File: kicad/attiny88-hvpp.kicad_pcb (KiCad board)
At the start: 2 copper layers, 77 x 58.7 mm, 15 parts, among them J1 12v_reg_left_neg, J2 12v_reg_right_pos, J3 purle_pi_left, J4 purle_pi_right, J5 ATTINY88_LEFT, J6 ATTINY88_RIGHT, Q1 MMBT3904, Q2 IRLML6402, Q3 MMBT3904, Q4 IRLML6402

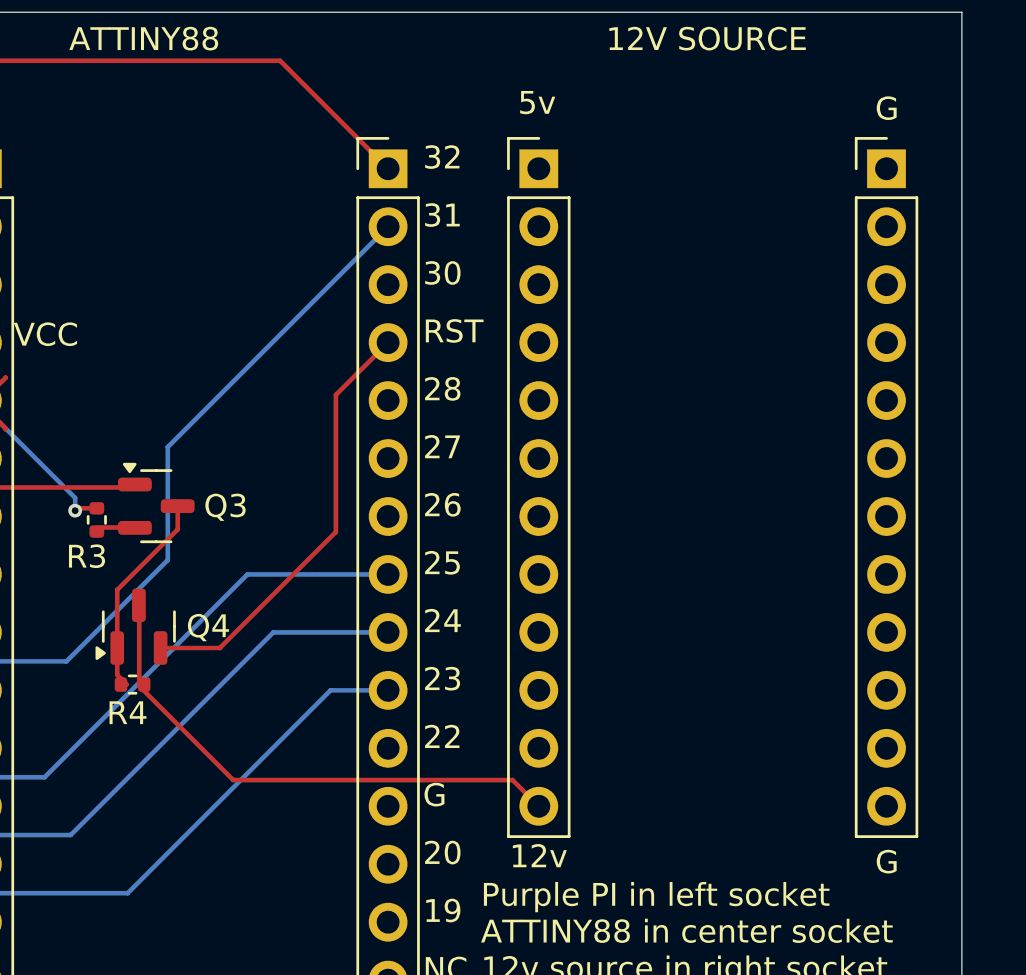
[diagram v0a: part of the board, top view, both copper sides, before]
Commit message: had left and right 12v switched
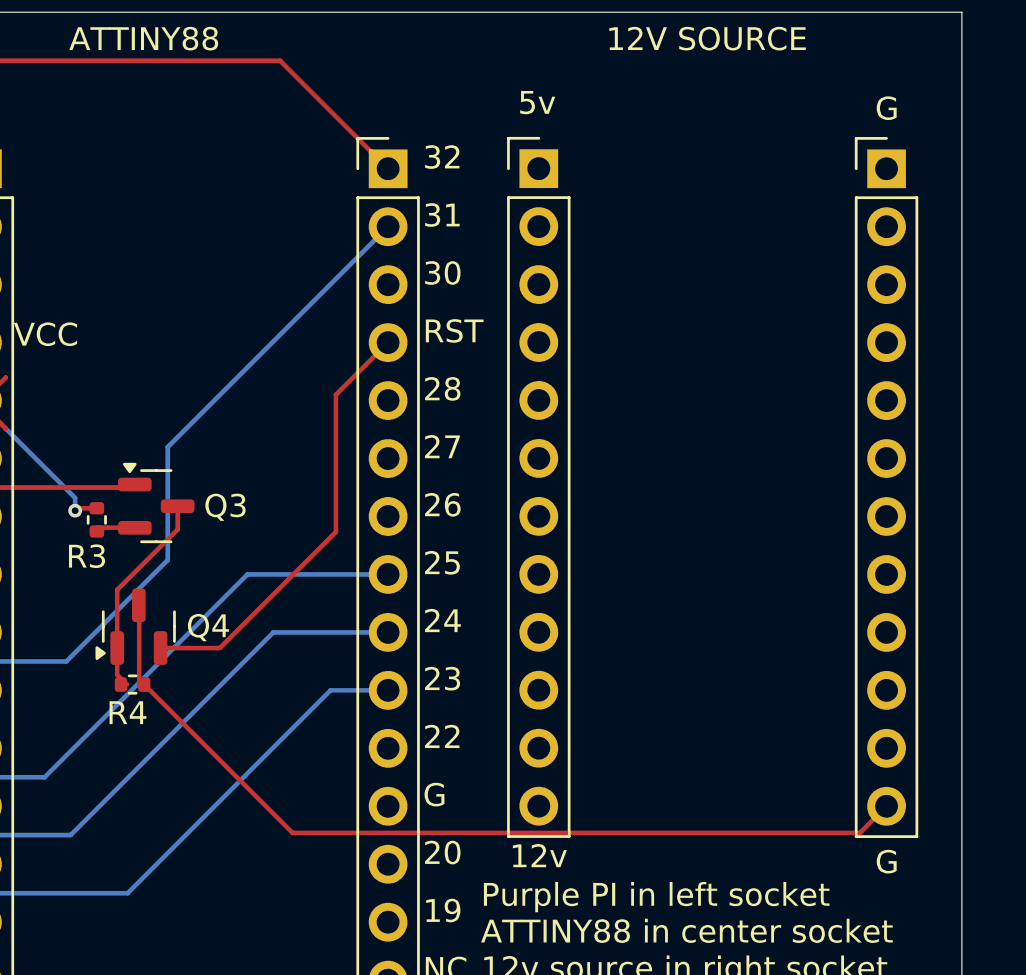
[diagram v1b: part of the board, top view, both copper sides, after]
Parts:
- moved J1 15.2 mm to (130.8, 55.9)
- moved J2 15.2 mm to (146.1, 55.9)
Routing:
- net /12v: track 23.2 -> 39.3 mm
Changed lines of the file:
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@@
   )
   (footprint "Connector_PinHeader_2.54mm:PinHeader_1x12_P2.54mm_Vertical" (layer "F.Cu")
-    (at 146.05 55.88)
+    (at 130.81 55.875)
     (descr "Through hole straight pin header, 1x12, 2.54mm pitch, single row")
     (tags "Through hole pin header THT 1x12 2.54mm single row")
@@
   )
   (footprint "Connector_PinHeader_2.54mm:PinHeader_1x12_P2.54mm_Vertical" (layer "F.Cu")
-    (at 130.81 55.88)
+    (at 146.05 55.88)
     (descr "Through hole straight pin header, 1x12, 2.54mm pitch, single row")
     (tags "Through hole pin header THT 1x12 2.54mm single row")
@@
   (segment (start 110.49 70.305) (end 106.335 66.15) (width 0.2) (layer "B.Cu") (net 2))
   (segment (start 113.2973 75.0218) (end 113.2973 78.5507) (width 0.2) (layer "F.Cu") (net 23))
-  (segment (start 113.2973 78.5507) (end 117.4166 82.67) (width 0.2) (layer "F.Cu") (net 23))
   (segment (start 113.284 75.0085) (end 113.2973 75.0218) (width 0.2) (layer "F.Cu") (net 23))
-  (segment (start 129.66 82.67) (end 130.81 83.82) (width 0.2) (layer "F.Cu") (net 23))
-  (segment (start 117.4166 82.67) (end 129.66 82.67) (width 0.2) (layer "F.Cu") (net 23))
+  (segment (start 120.020654 84.987654) (end 144.882346 84.987654) (width 0.2) (layer "F.Cu") (net 23))
+  (segment (start 113.519 78.486) (end 120.020654 84.987654) (width 0.2) (layer "F.Cu") (net 23))
+  (segment (start 144.882346 84.987654) (end 146.05 83.82) (width 0.2) (layer "F.Cu") (net 23))
   (segment (start 119.474 51.148) (end 124.206 55.88) (width 0.2) (layer "F.Cu") (net 24))
   (segment (start 78.392 51.148) (end 119.474 51.148) (width 0.2) (layer "F.Cu") (net 24))

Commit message: had left and right 12v switched
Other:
- board text added: "ATTINY88 HVPP REV003 2025-08-19"
- board text removed: "ATTINY88 HVPP REV002 2025-08-06"
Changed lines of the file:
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@@
   (gr_rect (start 72.39 49.022) (end 149.352 107.696)
     (stroke (width 0.05) (type default)) (fill none) (layer "Edge.Cuts"))
-  (gr_text "ATTINY88 HVPP\nREV002\n2025-08-06" (at 145.542 103.886) (layer "B.SilkS")
+  (gr_text "ATTINY88 HVPP\nREV003\n2025-08-19" (at 145.542 103.886) (layer "B.SilkS")
     (effects (font (size 1.5 1.5) (thickness 0.3) bold) (justify left bottom mirror))
   )
